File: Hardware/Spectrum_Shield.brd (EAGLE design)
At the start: 59.7 x 53.3 mm, 27 parts, among them IC1 MSGEQ7SOIC, IC2 MSGEQ7SOIC, U1 ARDUINO_R3_SHIELD

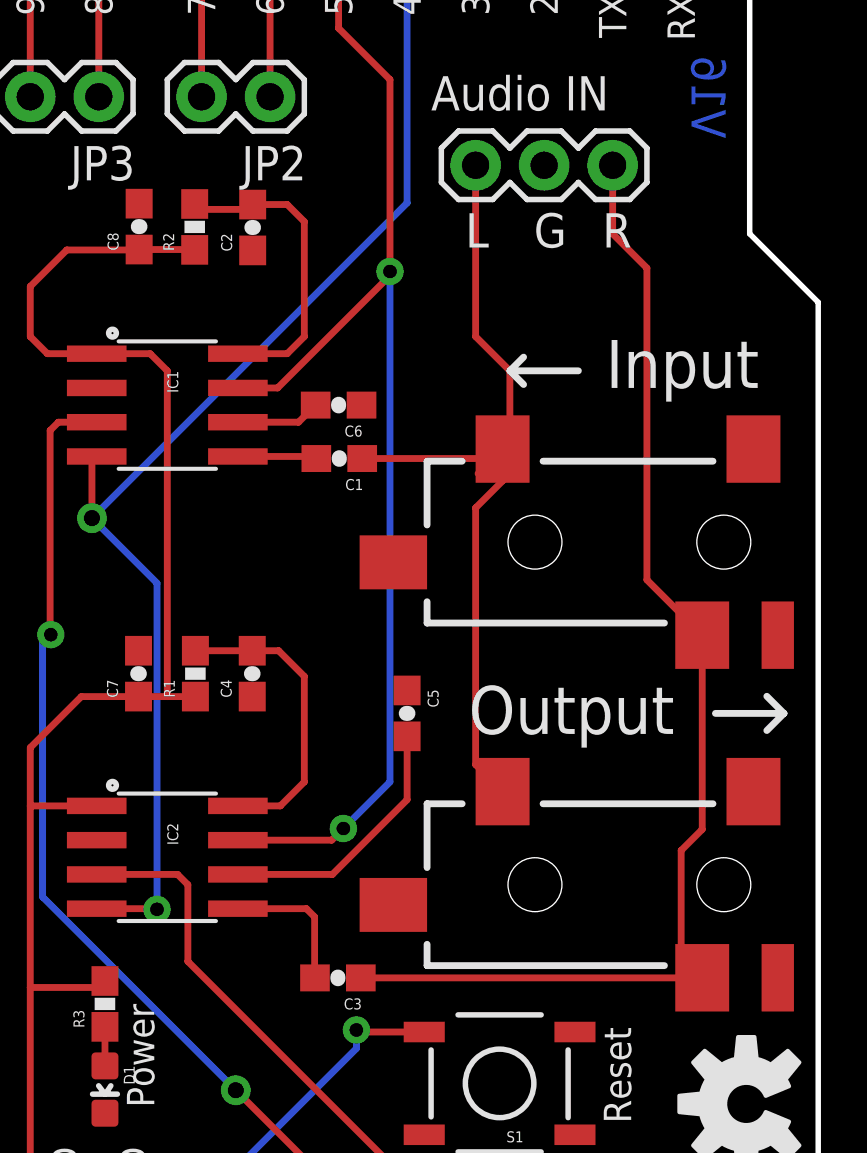
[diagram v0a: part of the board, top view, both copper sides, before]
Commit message: Fixed acid traps
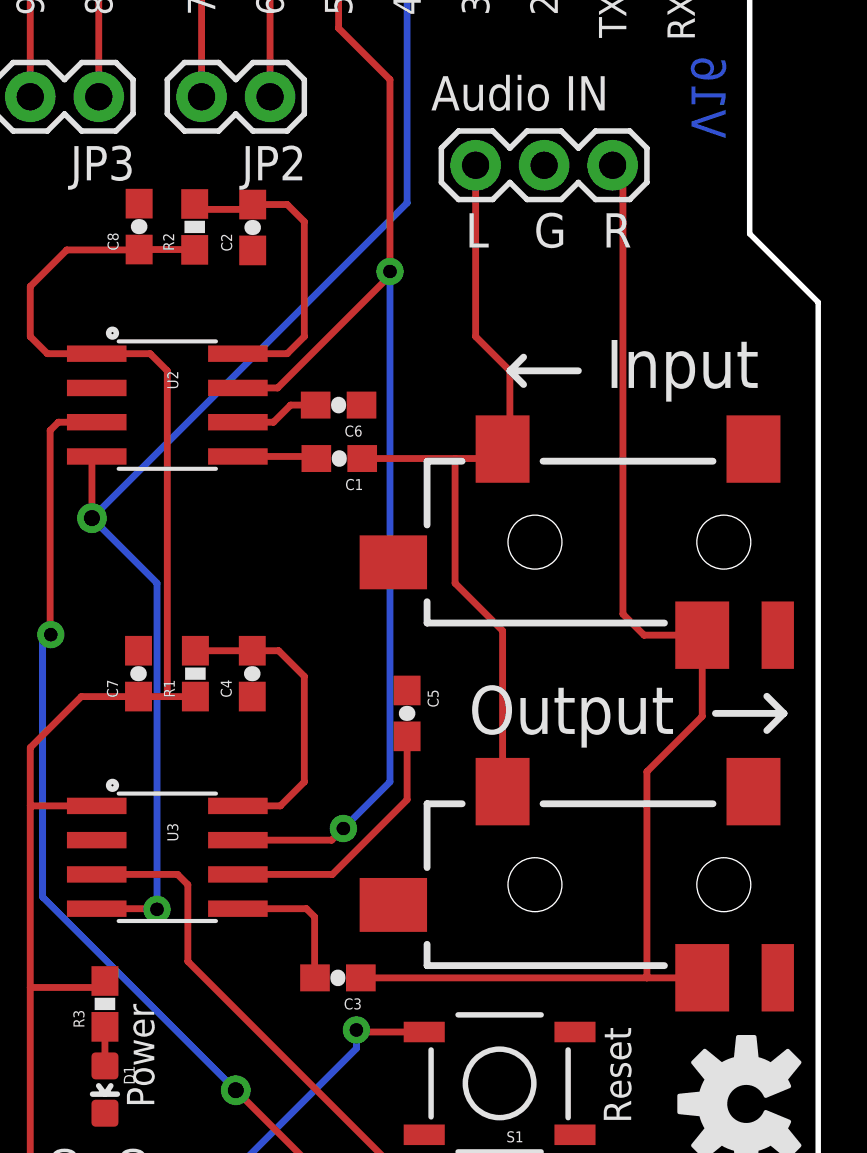
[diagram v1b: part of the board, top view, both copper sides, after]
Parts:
- renumbered IC1 to U2, IC2 to U3
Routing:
- net LEFT: track 31.3 -> 29.6 mm
- net RIGHT: track 45.8 -> 47.2 mm
